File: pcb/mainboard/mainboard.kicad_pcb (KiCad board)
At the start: 10 copper layers, 165 x 121 mm, 629 parts, among them J1 CONN_PCIE_PWR_8PIN, J10 FAN_01, J11 XILINX_JTAG, J12 JUMPER_0402_SPDT, J13 JUMPER_0402_SPDT, J14 RJ45, J15 PMOD_HOST, J16 SMPM, J17 SMPM, J18 SMPM, J19 SMPM, J2 CONN_IBC_MGMT, J20 SMPM, J21 SMPM, J22 SMPM, J23 SMPM, J24 SMPM, J25 SMPM, J26 SMPM, J27 0826-1G1T-23-F, J28 SMPM, J29 SMPM, J3 CONN_01X03, J30 SMPM, J31 SMPM, J32 SMPM, J33 SMPM, J34 SMPM, J35 SMPM, J36 SMPM, J37 SMPM, J38 SMPM, J39 SMPM, J4 CONN_01X05, J40 SMPM, J41 SMPM, J42 SMPM, J43 SMPM, J44 SMPM, J45 SMPM, J46 SMPM, J47 SMPM, J48 CONN_01X10, J5 XILINX_JTAG, J6 CONN_SFP_HOST, J7 SFP_CAGE, J8 FAN_01, J9 CONN_01X03, K1 RELAY_TE_HF3_96, K2 RELAY_TE_HF3_96, K3 RELAY_TE_HF3_96, K4 RELAY_TE_HF3_96, M1 960-23-23-F-AB-0, SW1 SWITCH, SW2 SWITCH, U1 STM32L031C6U6, U10 MAX40026, U11 MAX40026, U12 MAX40026, U13 MAX40026, U14 MAX40026, U15 MAX40026, U16 MAX40026, U17 MAX40026, U18 MAX40026, U19 MAX40026, U2 MYMGK1R812ERSR, U20 MAX40026, U21 DAC60508, U22 DAC60508, U23 STM32H735-UFBGA176-25, U24 AT24MAC402, U25 ADM3101E_QFN, U26 LMR70503, U27 SIT9121AI-2BF-XXS200.000000G, U28 SIT9121AI-2BF-XXS156.250000G, U29 HMC675LP3E, U3 MYMGK00504ERSR, U30 SIT9121AI-2BF-XXS200.000000G, U31 ECS-1612MV-250-CN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

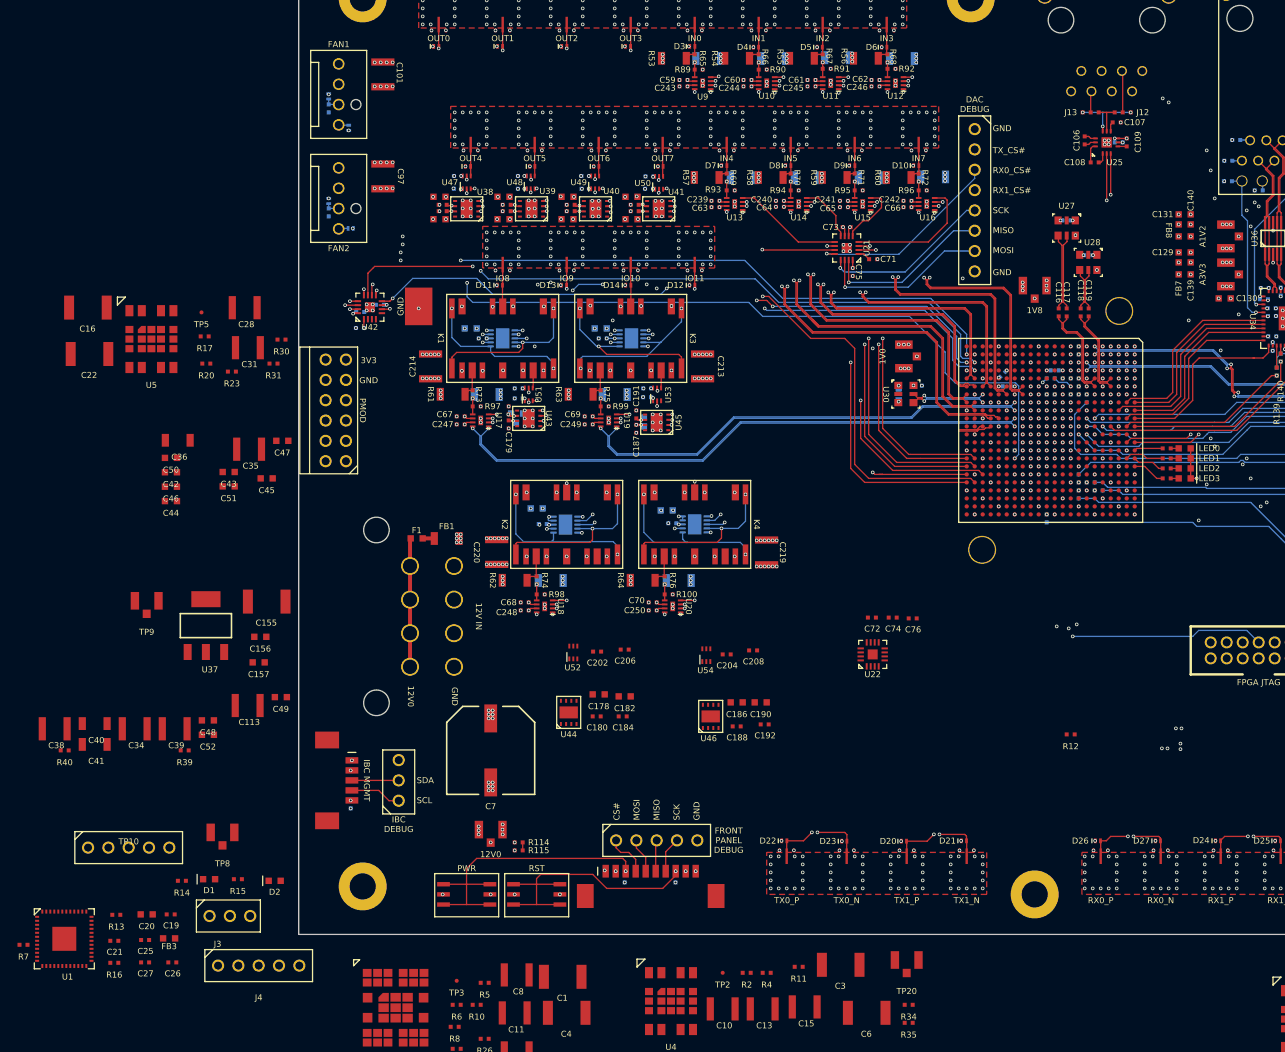
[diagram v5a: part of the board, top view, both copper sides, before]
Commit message: Initial routing of supervisor MCU
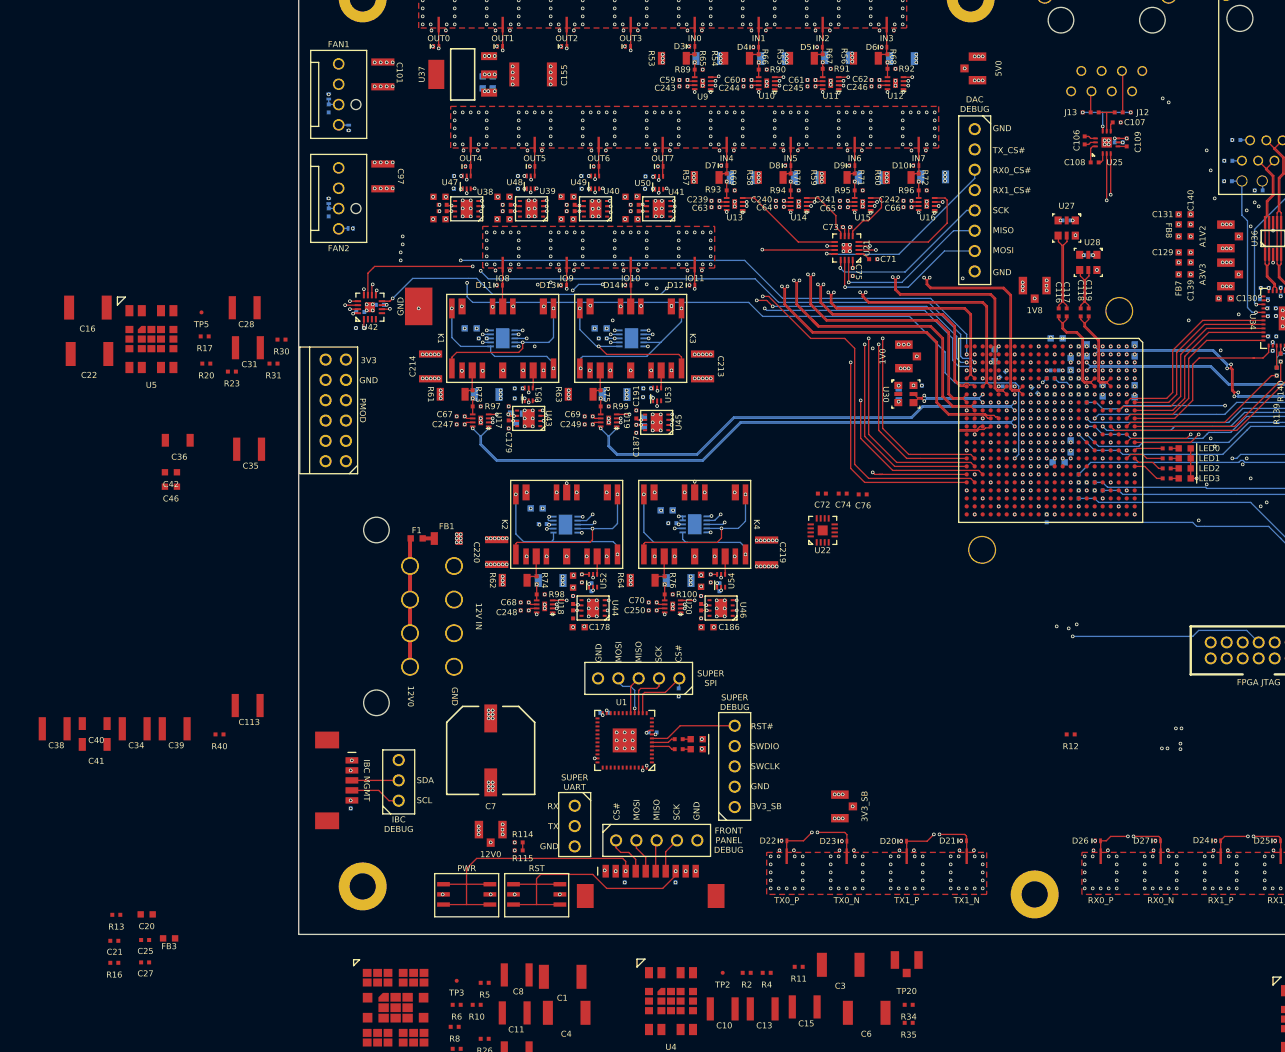
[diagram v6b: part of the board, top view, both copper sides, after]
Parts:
- C156, C157, C19, C206, C208, C26, C43, C44, C45, C47, C48, C49, C50, C51, C52, R39, R7: moved to B.Cu
- moved TP9 123.3 mm to (199.8, 32.8), turned to -90 degrees
- moved C50 120.8 mm to (219.5, 73.1), turned to -90 degrees
- moved C48 119.2 mm to (213.5, 68.0), turned to 90 degrees
- moved C52 117.1 mm to (209.8, 66.5), turned to 180 degrees
- moved R39 115.4 mm to (207.0, 73.0), turned to 135 degrees
- moved C51 114.5 mm to (219.5, 68.0), turned to 90 degrees
- moved C49 107.2 mm to (211.5, 69.7), turned to 90 degrees
- moved C43 105.3 mm to (211.5, 80.0), turned to -90 degrees
- moved C44 104.6 mm to (202.0, 68.6), turned to 90 degrees
- moved C47 102.7 mm to (215.5, 73.0), turned to -90 degrees
- moved C45 99.0 mm to (210.0, 82.0)
- moved R7 87.8 mm to (162.5, 110.8), turned to -90 degrees
- moved C157 78.2 mm to (139.2, 34.5), turned to -90 degrees
- moved TP8 77.3 mm to (182.8, 125.0), turned to 90 degrees
- moved U37 76.0 mm to (135.5, 33.5), turned to 90 degrees
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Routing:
- net /5V0: track 107.3 -> 264.2 mm, vias 13 -> 21
- net /GND: track 2260.3 -> 2362.4 mm, vias 1276 -> 1336
- net /3V3_SB: track 222.1 -> 266.0 mm, vias 8 -> 12
- net /12V0: track 271.1 -> 290.4 mm, vias 56 -> 64
- net /Output/VCCIO_11: track 0.00 -> 12.1 mm, vias 0 -> 4
- net /Output/VCCIO_9: track 0.00 -> 11.5 mm, vias 0 -> 4
- net /Power Supply/RST_N: track 0.00 -> 11.0 mm
- net /SUPER_SPI_CS_N: track 42.6 -> 51.7 mm
- net /SUPER_SPI_SCK: track 42.3 -> 48.8 mm
- net /SUPER_SPI_MOSI: track 39.4 -> 45.2 mm, vias 2 -> 3
- net /SUPER_SPI_MISO: track 40.4 -> 45.1 mm
- net /FPGA Support/GTX_1V8: track 42.4 -> 46.8 mm, vias 1 -> 2
- net /3V3: track 890.2 -> 893.8 mm, vias 153 -> 157
- net /Power Supply/SUPER_LED1: track 0.00 -> 3.02 mm
- net /Power Supply/SUPER_LED0: track 0.00 -> 2.99 mm
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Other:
- board text added: "3V3_SB"
- board text added: "5V0"
- board text added: "RST#"
- board text added: "RX"
- board text added: "SUPER DEBUG"
- board text added: "SUPER SPI"
- board text added: "SUPER UART"
- board text added: "SWCLK"
- board text added: "SWDIO"
- board text added: "TX"
- board text removed: "5V0 supply"
